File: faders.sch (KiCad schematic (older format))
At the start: 12 parts, among them U5 CD74HC4067M

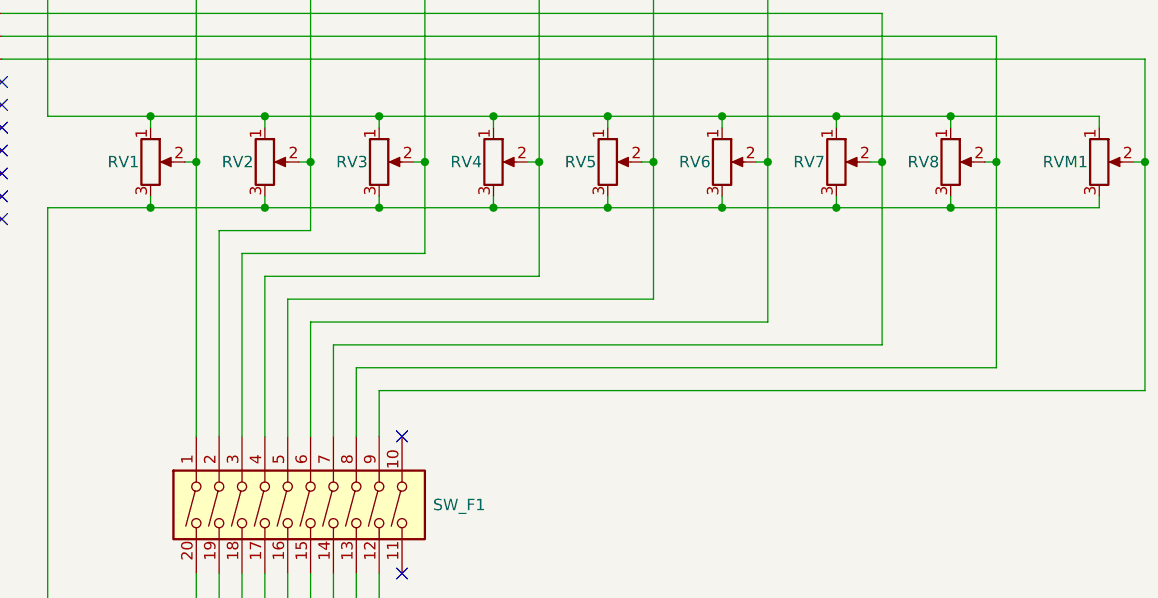
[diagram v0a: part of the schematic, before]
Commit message: Cleaning up and rerouting traces
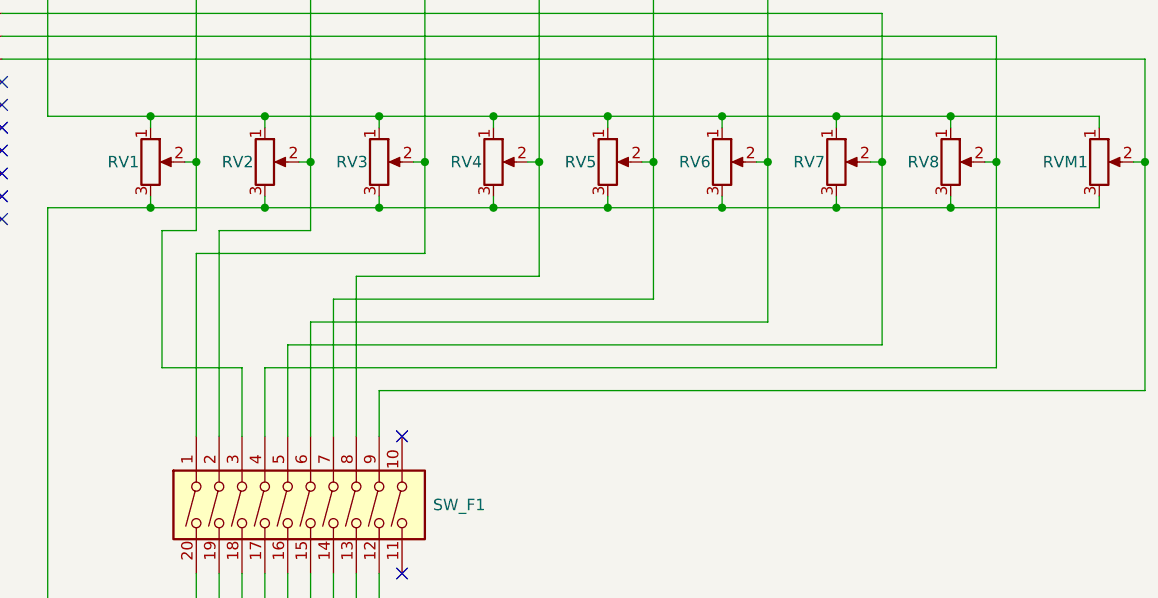
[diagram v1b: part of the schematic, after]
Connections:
- net at RV1.2, U5.9 (I0): now also SW_F1.3; no longer SW_F1.1
- net at RV3.2, U5.7 (I2): now also SW_F1.1; no longer SW_F1.3
- net at RV4.2, U5.6 (I3): now also SW_F1.8; no longer SW_F1.4
- net at RV5.2, U5.5 (I4): now also SW_F1.7; no longer SW_F1.5
- net at RV7.2, U5.3 (I6): now also SW_F1.5; no longer SW_F1.7
- net at RV8.2, U5.2 (I7): now also SW_F1.4; no longer SW_F1.8
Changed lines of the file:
@@
 	5050 2800 5050 3200
 Wire Wire Line
-	5050 3200 4250 3200
-Wire Wire Line
-	5550 3300 4350 3300
+	5550 3300 4750 3300
 Wire Wire Line
 	6050 2800 6050 3400
 Wire Wire Line
-	6050 3400 4450 3400
+	6050 3400 4650 3400
 Wire Wire Line
 	6550 2800 6550 3500
@@
 	7050 2800 7050 3600
 Wire Wire Line
-	7050 3600 4650 3600
-Wire Wire Line
 	7550 2800 7550 3700
-Wire Wire Line
-	7550 3700 4750 3700
-Wire Wire Line
-	4050 2800 4050 4000
-Connection ~ 4050 2800
-Wire Wire Line
-	4150 3100 4150 4000
-Wire Wire Line
-	4250 3200 4250 4000
-Wire Wire Line
-	4350 3300 4350 4000
-Wire Wire Line
-	4450 3400 4450 4000
-Wire Wire Line
-	4550 3500 4550 4000
-Wire Wire Line
-	4650 3600 4650 4000
-Wire Wire Line
-	4750 3700 4750 4000
 Wire Wire Line
 	8200 2800 8200 3800
@@
 Text GLabel 2000 2450 0    50   Input ~ 0
 S3
-Wire Wire Line
-	4850 3800 4850 4000
 NoConn ~ 4950 4000
 NoConn ~ 4950 4600
@@
 $EndComp
 Wire Wire Line
-	4850 3800 8200 3800
-Wire Wire Line
 	8000 3000 7350 3000
 Connection ~ 7350 3000
@@
 Wire Wire Line
 	8000 2600 7350 2600
+Wire Wire Line
+	4050 3200 4050 4000
+Wire Wire Line
+	4050 3200 5050 3200
+Wire Wire Line
+	4150 3100 4150 4000
+Wire Wire Line
+	4050 2800 4050 3100
+Wire Wire Line
+	4050 3100 3900 3100
+Wire Wire Line
+	3900 3100 3900 3700
+Wire Wire Line
+	3900 3700 4250 3700
+Wire Wire Line
+	4250 3700 4250 4000
+Connection ~ 4050 2800
+Wire Wire Line
+	4850 3800 8200 3800
+Wire Wire Line
+	4850 3800 4850 4000
+Wire Wire Line
+	4350 3700 4350 4000
+Wire Wire Line
+	4350 3700 7550 3700
+Wire Wire Line
+	4450 3600 4450 4000
+Wire Wire Line
+	4450 3600 7050 3600
+Wire Wire Line
+	4550 3500 4550 4000
+Wire Wire Line
+	4650 3400 4650 4000
+Wire Wire Line
+	4750 3300 4750 4000
 $EndSCHEMATC

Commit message: Revert "Cleaning up and rerouting traces"
This reverts commit c6a633449036ff81e758f695dc37825436db76d9.
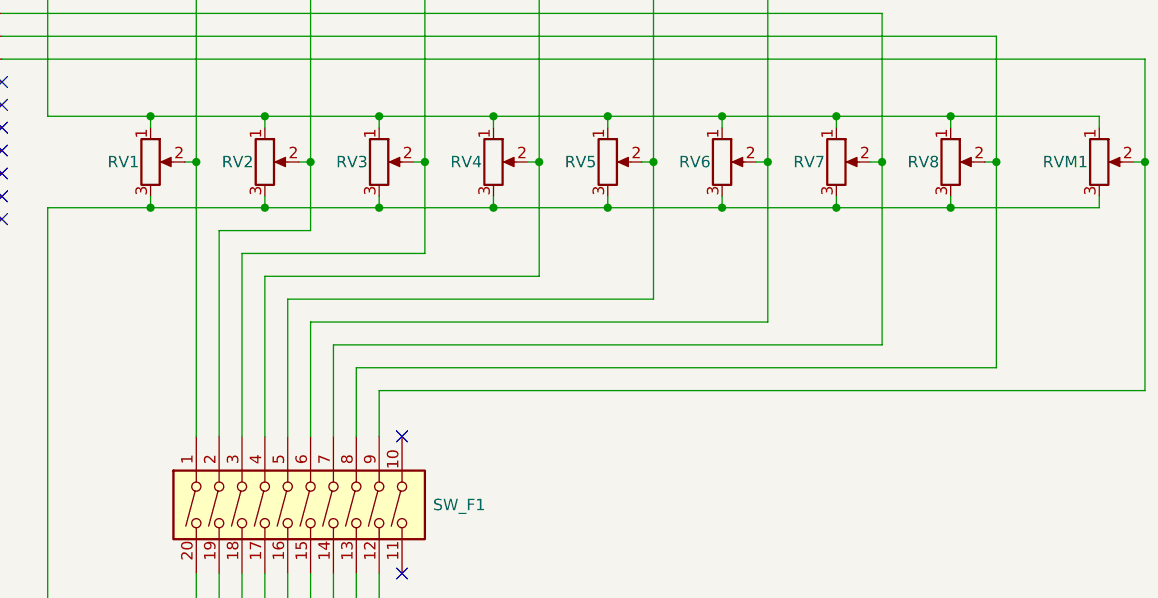
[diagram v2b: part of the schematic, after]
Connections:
- net at RV3.2, U5.7 (I2): now also SW_F1.3; no longer SW_F1.1
- net at RV1.2, U5.9 (I0): now also SW_F1.1; no longer SW_F1.3
- net at RV8.2, U5.2 (I7): now also SW_F1.8; no longer SW_F1.4
- net at RV7.2, U5.3 (I6): now also SW_F1.7; no longer SW_F1.5
- net at RV5.2, U5.5 (I4): now also SW_F1.5; no longer SW_F1.7
- net at RV4.2, U5.6 (I3): now also SW_F1.4; no longer SW_F1.8
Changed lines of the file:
@@
 	5050 2800 5050 3200
 Wire Wire Line
-	5550 3300 4750 3300
+	5050 3200 4250 3200
+Wire Wire Line
+	5550 3300 4350 3300
 Wire Wire Line
 	6050 2800 6050 3400
 Wire Wire Line
-	6050 3400 4650 3400
+	6050 3400 4450 3400
 Wire Wire Line
 	6550 2800 6550 3500
@@
 	7050 2800 7050 3600
 Wire Wire Line
+	7050 3600 4650 3600
+Wire Wire Line
 	7550 2800 7550 3700
+Wire Wire Line
+	7550 3700 4750 3700
+Wire Wire Line
+	4050 2800 4050 4000
+Connection ~ 4050 2800
+Wire Wire Line
+	4150 3100 4150 4000
+Wire Wire Line
+	4250 3200 4250 4000
+Wire Wire Line
+	4350 3300 4350 4000
+Wire Wire Line
+	4450 3400 4450 4000
+Wire Wire Line
+	4550 3500 4550 4000
+Wire Wire Line
+	4650 3600 4650 4000
+Wire Wire Line
+	4750 3700 4750 4000
 Wire Wire Line
 	8200 2800 8200 3800
@@
 Text GLabel 2000 2450 0    50   Input ~ 0
 S3
+Wire Wire Line
+	4850 3800 4850 4000
 NoConn ~ 4950 4000
 NoConn ~ 4950 4600
@@
 $EndComp
 Wire Wire Line
+	4850 3800 8200 3800
+Wire Wire Line
 	8000 3000 7350 3000
 Connection ~ 7350 3000
@@
 Wire Wire Line
 	8000 2600 7350 2600
-Wire Wire Line
-	4050 3200 4050 4000
-Wire Wire Line
-	4050 3200 5050 3200
-Wire Wire Line
-	4150 3100 4150 4000
-Wire Wire Line
-	4050 2800 4050 3100
-Wire Wire Line
-	4050 3100 3900 3100
-Wire Wire Line
-	3900 3100 3900 3700
-Wire Wire Line
-	3900 3700 4250 3700
-Wire Wire Line
-	4250 3700 4250 4000
-Connection ~ 4050 2800
-Wire Wire Line
-	4850 3800 8200 3800
-Wire Wire Line
-	4850 3800 4850 4000
-Wire Wire Line
-	4350 3700 4350 4000
-Wire Wire Line
-	4350 3700 7550 3700
-Wire Wire Line
-	4450 3600 4450 4000
-Wire Wire Line
-	4450 3600 7050 3600
-Wire Wire Line
-	4550 3500 4550 4000
-Wire Wire Line
-	4650 3400 4650 4000
-Wire Wire Line
-	4750 3300 4750 4000
 $EndSCHEMATC
